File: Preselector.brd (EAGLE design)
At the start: 183 x 137.8 mm, 266 parts, among them IC58 LMZ31707RVQ, Q2 FDV303N, X1 0733660061, X10 0733660061, X11 0733660061, X12 0733660061, X13 0733660061, X14 0733660061, X15 0733660061, X16 0733660061, X17 0733660061, X18 0733660061, X19 0733660061, X2 0733660061, X20 0733660061, X21 0733660061, X22 0733660061, X23 0733660061, X24 0733660061, X25 0733660061, X26 0733660061, X27 0733660061, X28 0733660061, X29 0733660061, X3 0733660061, X30 0733660061, X31 0733660061, X32 0733660061, X4 0733660061, X5 0733660061, X6 0733660061, X7 0733660061, X8 0733660061, X9 0733660061

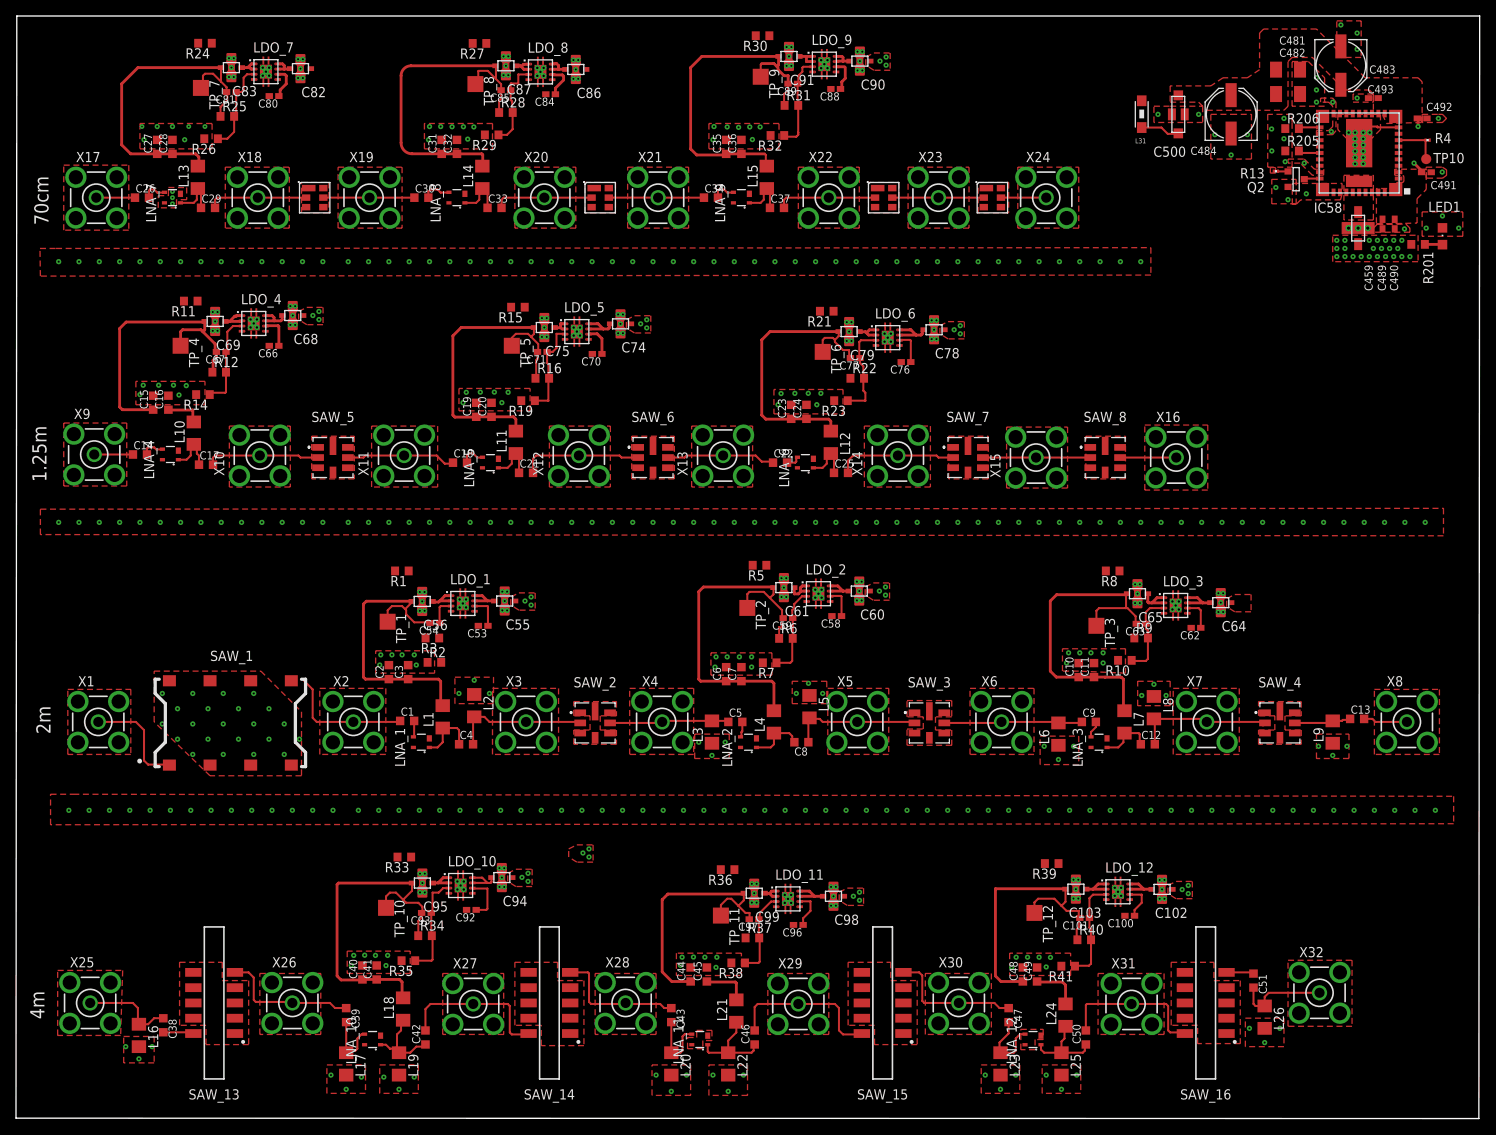
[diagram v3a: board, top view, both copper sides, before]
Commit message: routed some stuff, added +5V3 polygons.
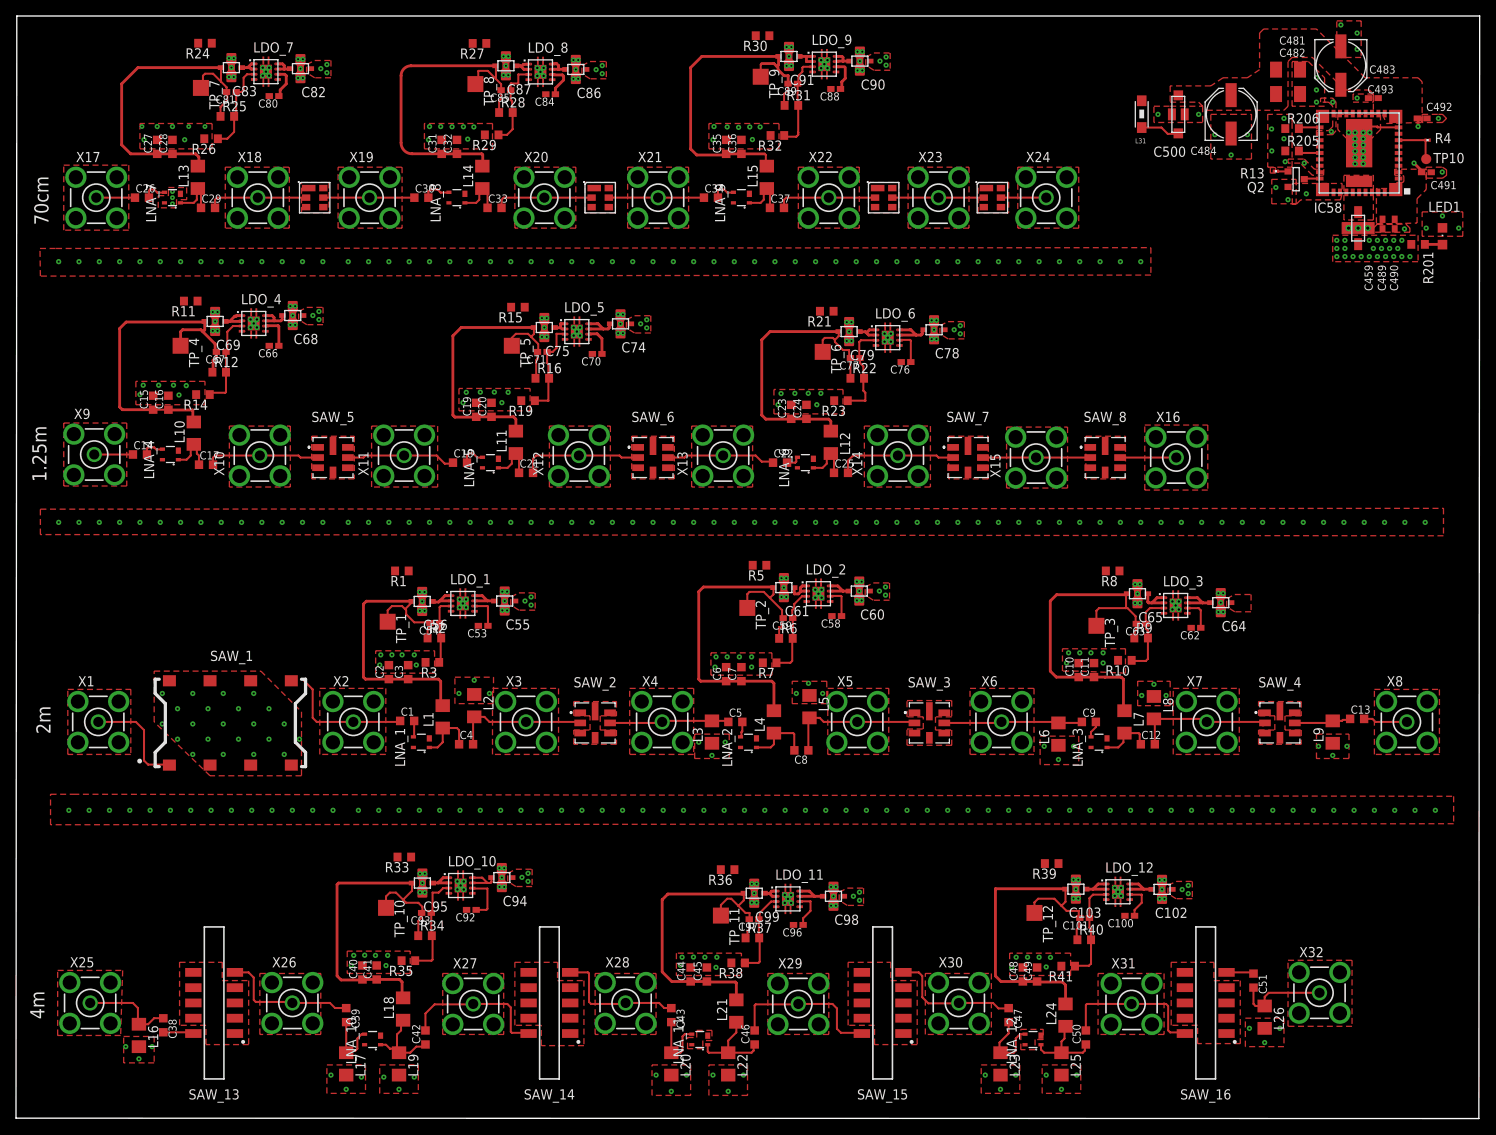
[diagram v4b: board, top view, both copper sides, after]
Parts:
- moved R2 3.05 mm to (52.3, 60.0)
- moved R3 3.05 mm to (52.0, 57.0)
- moved C8 1.02 mm to (98.2, 46.0)
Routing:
- net N$12: track 3.55 -> 9.23 mm
- net LDO_11_5V: track 38.1 -> 42.7 mm
- net LDO_6_5V: track 37.7 -> 40.2 mm
- net LDO_1_5V: track 37.8 -> 39.8 mm
- net LDO_4_5V: track 41.8 -> 43.7 mm
- net LDO_3_5V: track 42.3 -> 44.2 mm
- net LDO_12_5V: track 43.3 -> 45.1 mm
- net LNA_2_OUT: track 6.67 -> 8.37 mm
- net SAW_3_IN: track 16.8 -> 17.5 mm
- net SAW_14_IN: track 19.4 -> 18.8 mm
- added copper zone on layer 1, net +5V1
- added copper zone on layer 1, net +5V4
- removed copper zone on layer 1, net +5V2

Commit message: All components should be connected to ground as well as all pre_pwr wires have been routed. 4 air wires remain...
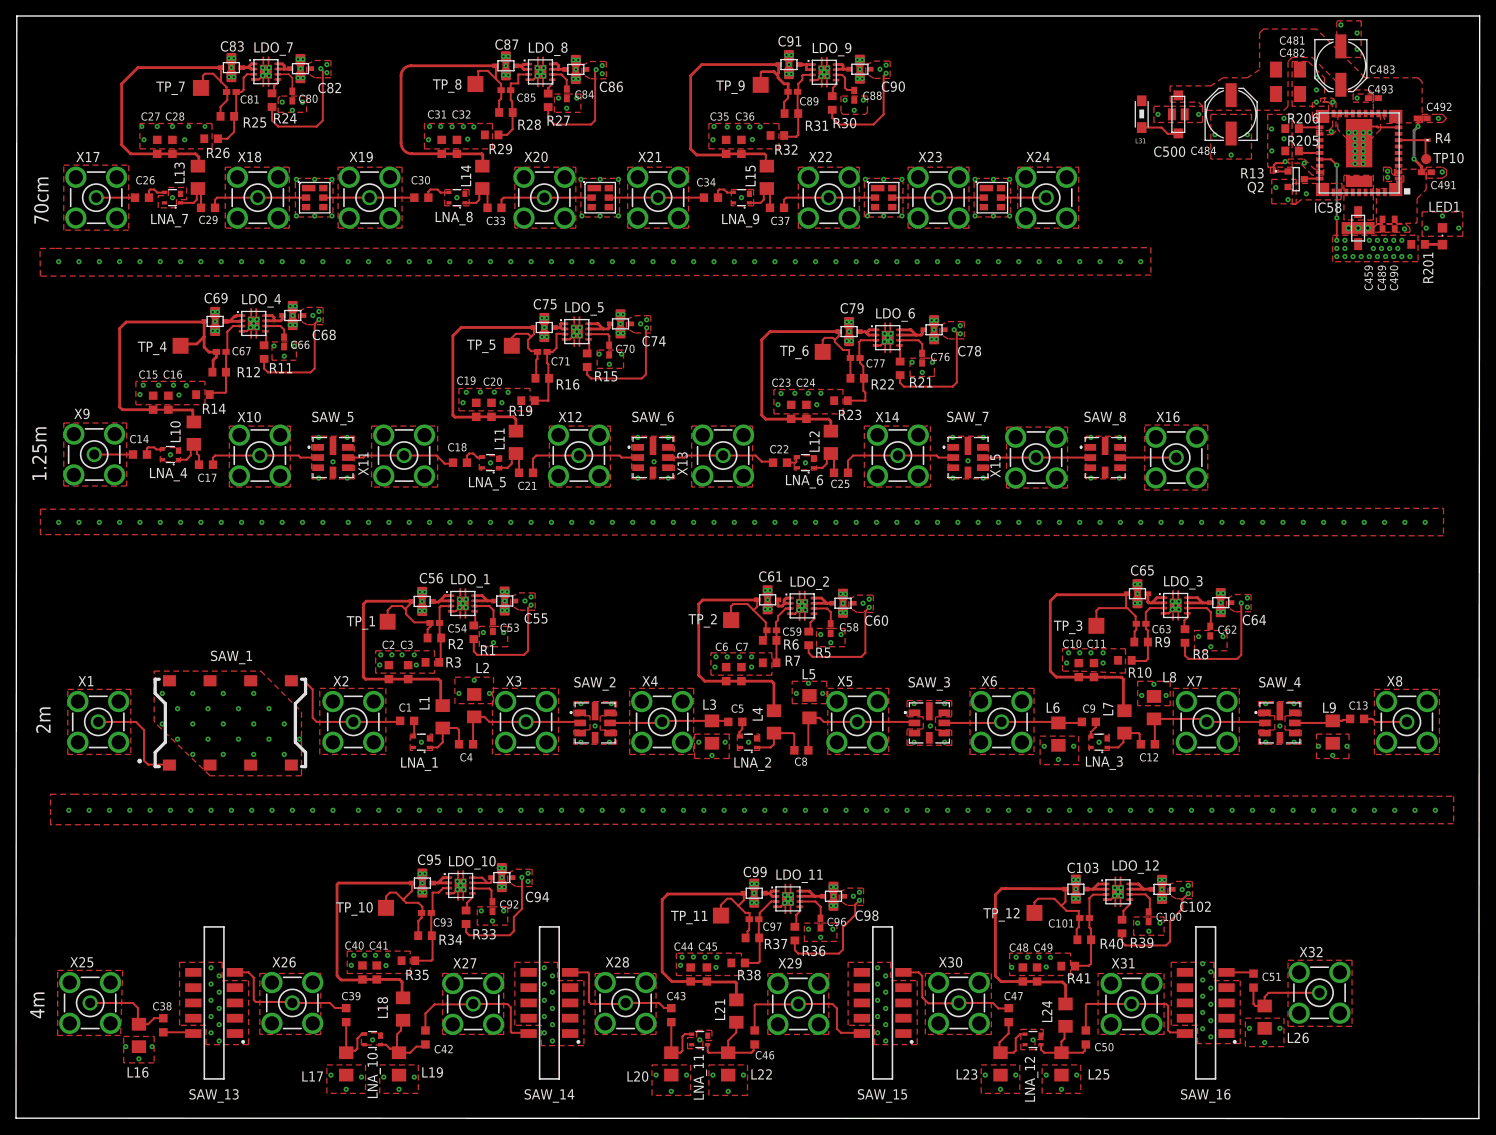
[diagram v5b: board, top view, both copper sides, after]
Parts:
- moved R8 12.2 mm to (146.1, 60.3), turned to 90 degrees
- moved R30 12.1 mm to (102.0, 126.9), turned to 90 degrees
- moved R1 11.8 mm to (57.2, 60.7), turned to 90 degrees
- moved R39 11.8 mm to (138.3, 24.0), turned to 90 degrees
- moved R21 11.6 mm to (110.5, 93.7), turned to 90 degrees
- moved R36 11.6 mm to (97.4, 23.1), turned to 90 degrees
- moved R11 11.2 mm to (31.0, 95.8), turned to 90 degrees
- moved R27 11.1 mm to (66.5, 127.2), turned to 90 degrees
- moved R5 11.0 mm to (99.1, 60.0), turned to 90 degrees
- moved R24 11.0 mm to (32.0, 127.3), turned to 90 degrees
- moved R15 10.9 mm to (71.4, 94.7), turned to 90 degrees
- moved R33 10.8 mm to (56.3, 25.1), turned to 90 degrees
- moved C96 2.78 mm to (100.6, 24.4), turned to 270 degrees
- moved C92 2.67 mm to (59.6, 26.4), turned to 270 degrees
- moved C59 2.54 mm to (94.5, 61.0)
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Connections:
- removed net PRE_PWR: LDO_1.5, LDO_10.5, LDO_11.5, LDO_12.5, LDO_2.5, LDO_3.5, LDO_4.5, LDO_5.5, LDO_6.5, LDO_7.5, LDO_8.5, LDO_9.5, R1.2, R11.2, R15.2, R21.2, R24.2, R27.2, R30.2, R33.2, R36.2, R39.2, R5.2, R8.2
- new net PRE_PWR_1: LDO_1.5, R1.2
- new net PRE_PWR_10: LDO_10.5, R33.2
- new net PRE_PWR_11: LDO_11.5, R36.2
- new net PRE_PWR_12: LDO_12.5, R39.2
- new net PRE_PWR_2: LDO_2.5, R5.2
- new net PRE_PWR_3: LDO_3.5, R8.2
- new net PRE_PWR_4: LDO_4.5, R11.2
- new net PRE_PWR_5: LDO_5.5, R15.2
- new net PRE_PWR_6: LDO_6.5, R21.2
- new net PRE_PWR_7: LDO_7.5, R24.2
- new net PRE_PWR_8: LDO_8.5, R27.2
- new net PRE_PWR_9: LDO_9.5, R30.2
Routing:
- net +5V3: track 0.00 -> 186.8 mm, vias 50 -> 61
- net GND: track 0.00 -> 45.4 mm, vias 358 -> 506
- net N$199: track 4.47 -> 10.4 mm
- net LDO_2_5V: track 46.3 -> 41.0 mm
- net N$16: track 11.2 -> 7.83 mm
- net PRE_PWR_12: track 0.00 -> 2.95 mm
- net PRE_PWR_11: track 0.00 -> 2.80 mm
- net PRE_PWR_2: track 0.00 -> 2.54 mm
- net PRE_PWR_10: track 0.00 -> 2.50 mm
- net PRE_PWR_9: track 0.00 -> 2.24 mm
- net PRE_PWR_3: track 0.00 -> 2.21 mm
- net PRE_PWR_7: track 0.00 -> 2.06 mm
- net PRE_PWR_6: track 0.00 -> 2.01 mm
- net PRE_PWR_8: track 0.00 -> 1.97 mm
- net N$62: track 5.83 -> 3.90 mm
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- removed copper zone on layer 1, net +5V1
- removed copper zone on layer 1, net +5V4
- removed copper zone on layer 1, net N$7

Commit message: Found 1 airwire, 3 left.
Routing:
- net +13.8V_SW_FIL: track 7.37 -> 10.3 mm
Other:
- board text removed: "You must do a "poly 'gnd" each polygon to associate it with ground."
- board text removed: "You must do a "via 'gnd" command to make the via a ground otherwise you will see circles in the polygon"
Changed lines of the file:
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@@
 <vertex x="6.096" y="45.466"/>
 </polygon>
-<text x="33.274" y="147.828" size="1.778" layer="100">You must do a "poly 'gnd" each polygon to associate it with ground.</text>
-<text x="32.766" y="144.526" size="1.778" layer="100">You must do a "via 'gnd" command to make the via a ground otherwise you will see circles in the polygon</text>
 </plain>
 <attributes>
@@
 <wire x1="175.26" y1="123.952" x2="175.26" y2="124.876" width="0.3556" layer="1"/>
 <wire x1="175.26" y1="124.876" x2="175.168" y2="124.968" width="0.3556" layer="1"/>
-<wire x1="172.469" y1="116.075" x2="172.819" y2="118.25" width="0" layer="19" extent="1-1"/>
+<wire x1="172.819" y1="118.25" x2="175.6884" y2="118.25" width="0.254" layer="1"/>
+<wire x1="175.6884" y1="118.25" x2="175.7014" y2="118.237" width="0.254" layer="1"/>
 </signal>
 <signal name="N$196">

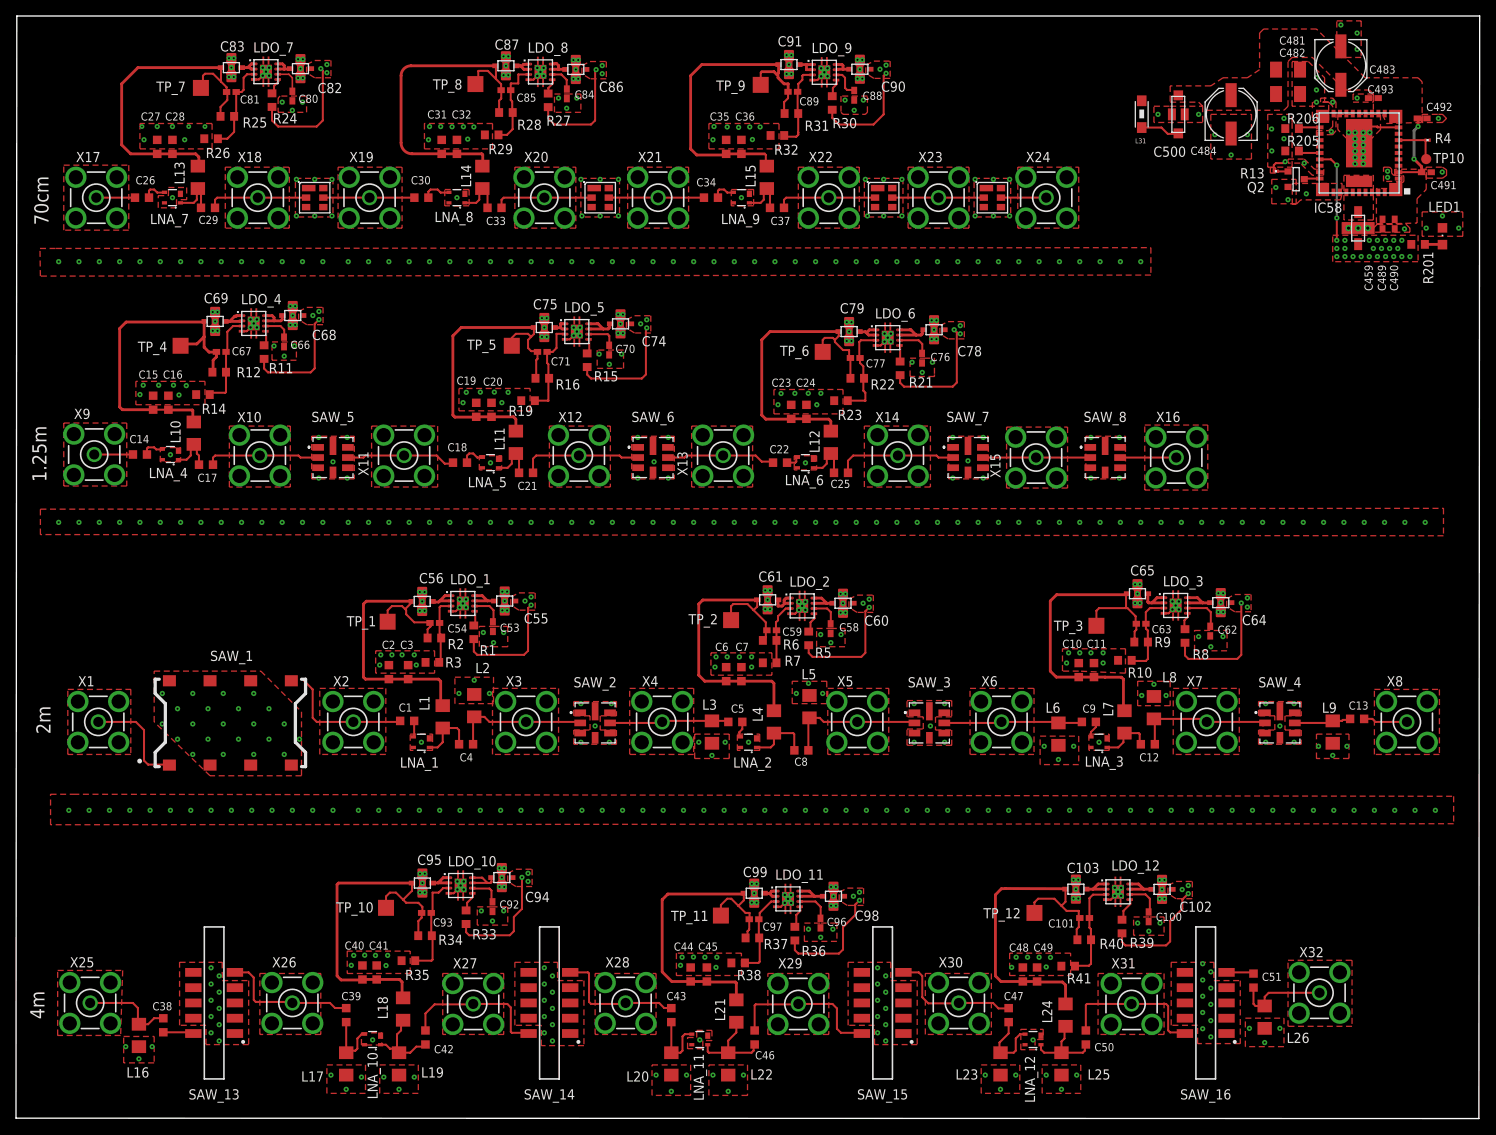
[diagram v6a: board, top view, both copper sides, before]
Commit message: Finished board, 0 airwires left. Check for polygon shorts.
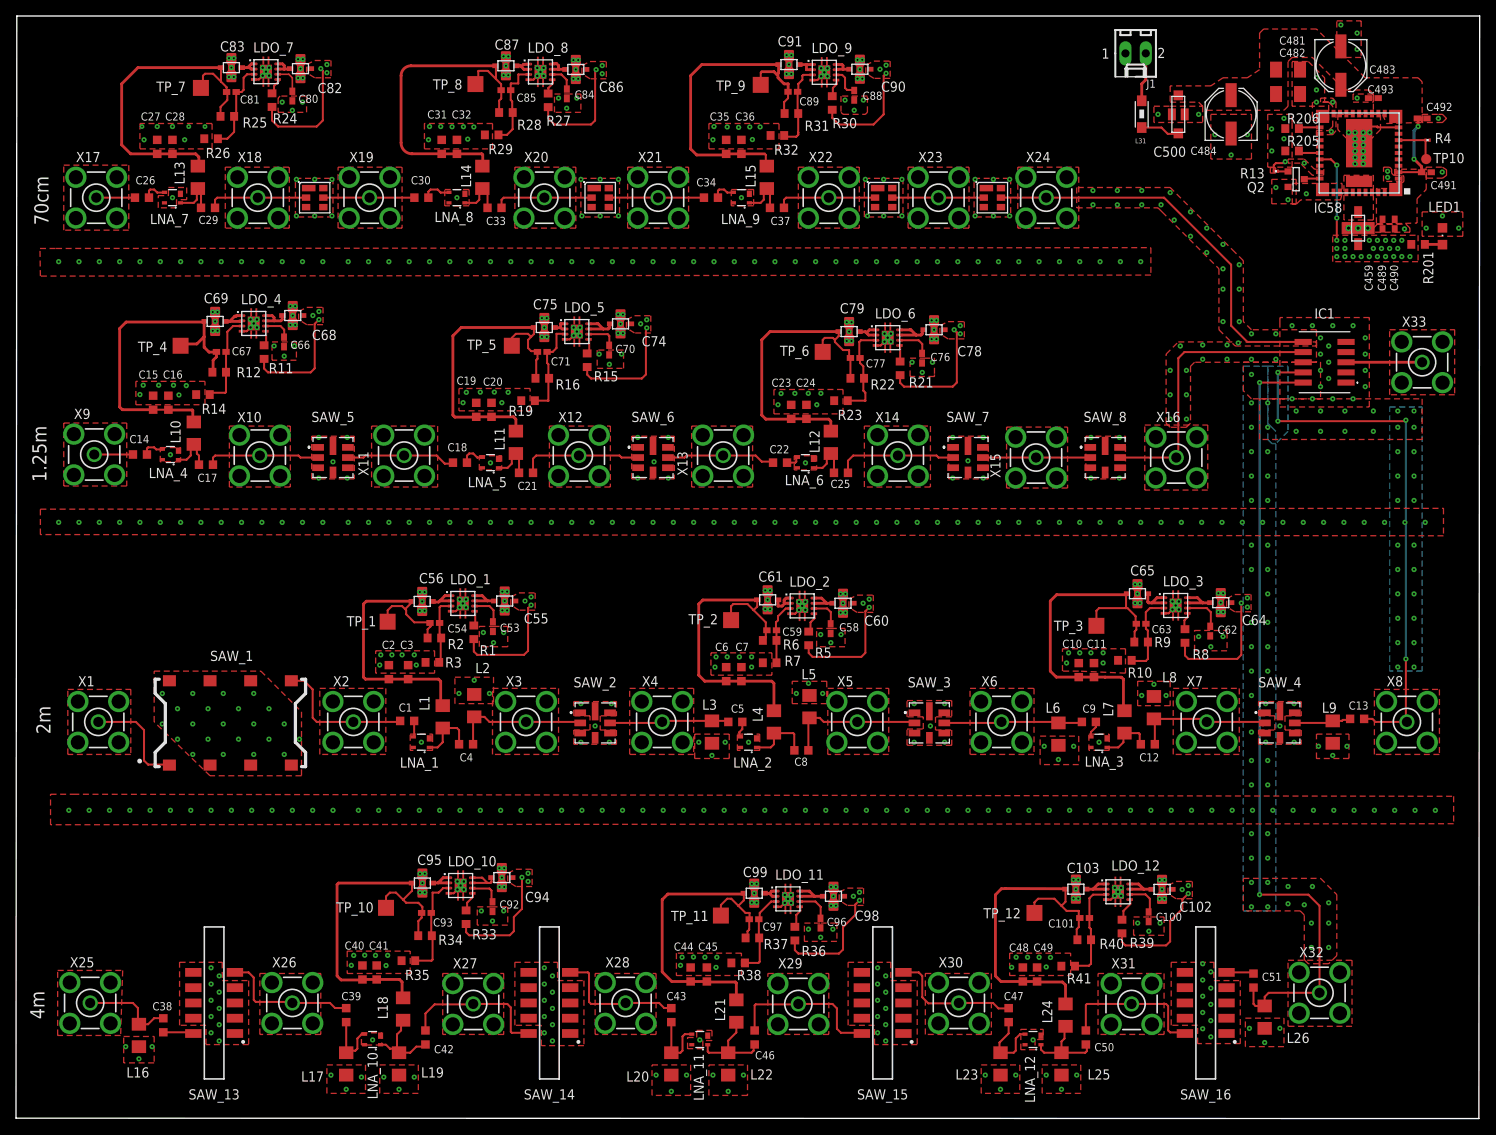
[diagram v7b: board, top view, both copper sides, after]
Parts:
- added IC1: SCA-4-10+, SeniorDesign:SCA-4-10+
- added J1: 22-27-2021-02, con-molex:6410-02
- added X33: 0733660061, con-coax:BU-SMA-V
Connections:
- new net PRE_OUT: IC1.3, X33.1
- net +13.8V_TPS: now also J1.2
- net 1.25_RF_OUT: now also IC1.7
- net 2M_RF_OUT: now also IC1.9
- net 4M_RF_OUT: now also IC1.10
- net 70CM_RF_OUT: now also IC1.6
- net GND: now also IC1.1, IC1.2, IC1.4, IC1.5, IC1.8, J1.1, X33.2, X33.3, X33.4, X33.5
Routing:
- net 4M_RF_OUT: track 11.8 -> 100.2 mm, vias 0 -> 2
- net 2M_RF_OUT: track 5.51 -> 68.6 mm, vias 0 -> 4
- net 70CM_RF_OUT: track 5.66 -> 49.7 mm
- net 1.25_RF_OUT: track 7.03 -> 35.5 mm
- net PRE_OUT: track 0.00 -> 9.51 mm
- net +13.8V_TPS: track 0.00 -> 6.13 mm
- net SAW_1_OUT: track 16.3 -> 17.9 mm
- net GND: vias 506 -> 636
- added copper zone on layer 16, net GND
